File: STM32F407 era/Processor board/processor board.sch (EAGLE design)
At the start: 27 parts, among them Q1 8 MHz, X1 MINI-USB-SCHIELD-32005-201

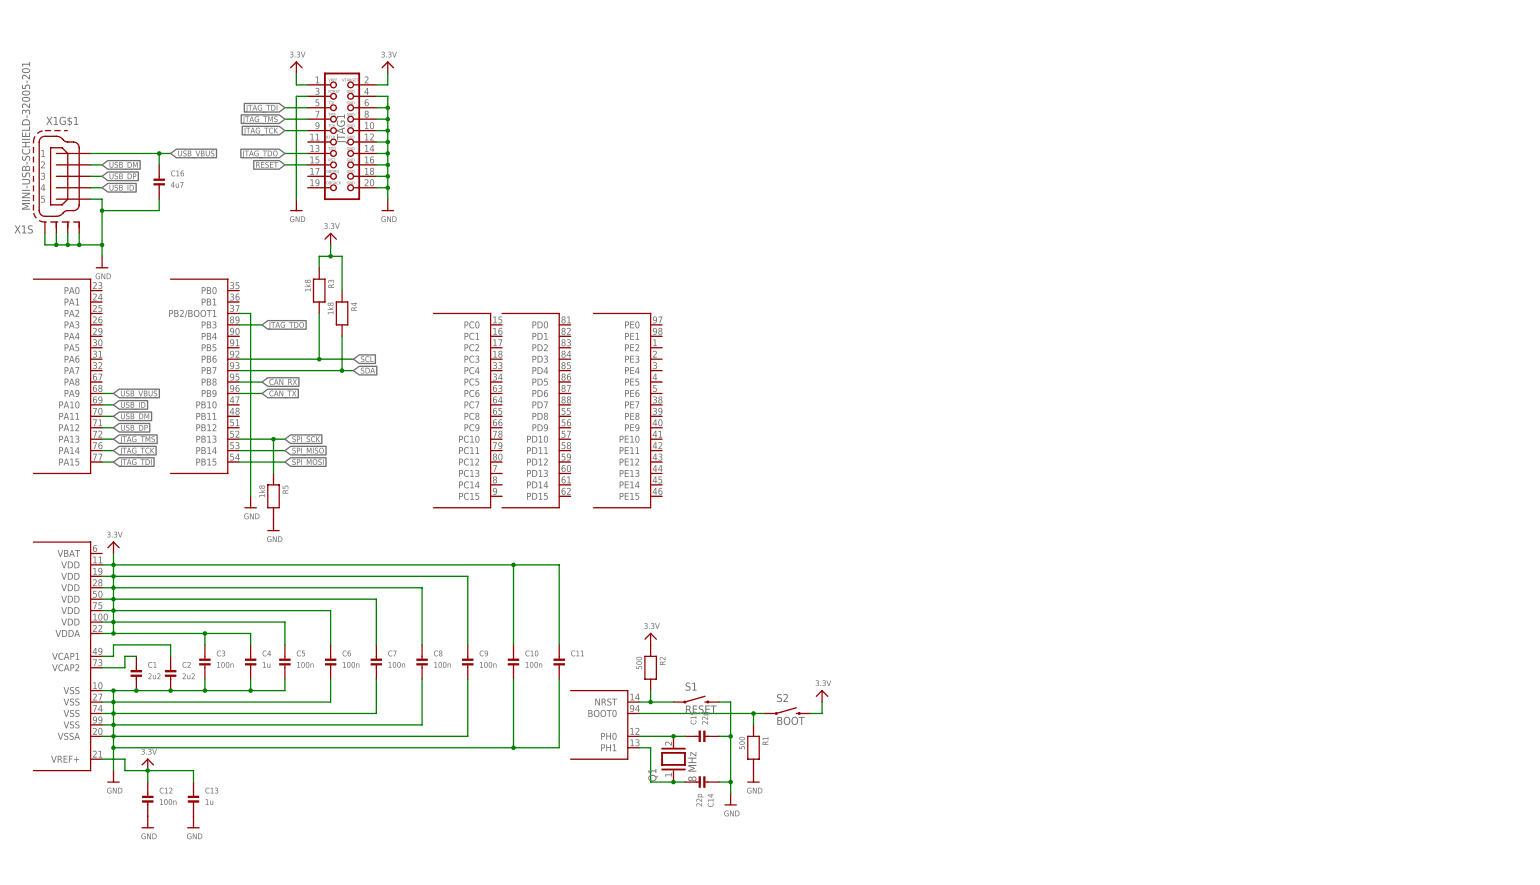
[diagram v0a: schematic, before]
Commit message: continued work on processor board
started doing the layout for the board and startet to add the
interfacing pin rows.
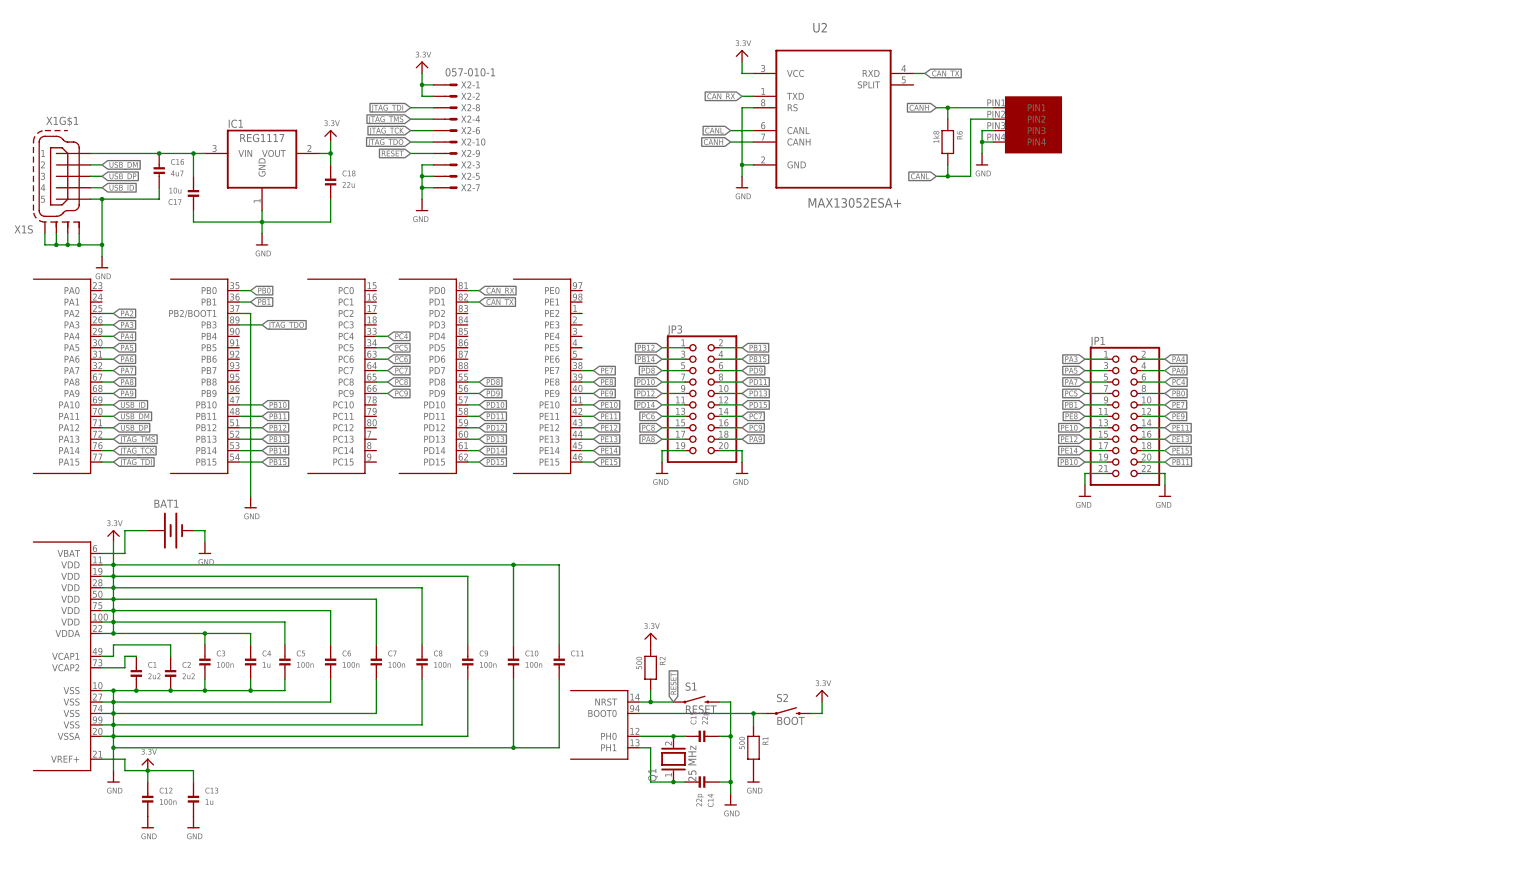
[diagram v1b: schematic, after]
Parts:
- removed JTAG1: JTAG-ARM, microbuilder:JTAG-ARM
- removed R3, R4, R5: 1k8, microbuilder:RESISTOR_0402MP
- added BAT1: (no value), SparkFun-Electromechanical:BATTERY12PTH
- added C17: 10u, microbuilder:CAP_CERAMIC_0603MP
- added C18: 22u, microbuilder:CAP_CERAMIC_0603MP
- added IC1: REG1117, burr-brown:REG1117
- added JP1: (no value), pinhead:PINHD-2X11
- added JP3: (no value), pinhead:PINHD-2X10
- added R6: 1k8, microbuilder:RESISTOR_0402MP
- added U$23: MICROFIT4, unicorn:MICROFIT4
- added U2: MAX13052ESA+, Maxim_By_element14_Batch_1:MAX13052ESA+
- added X2: 057-010-1, con-panduit:057-010-1
- Q1: value 8 MHz -> 25 MHz
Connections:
- removed net N$5: R2.2, S1.1, U1G$7.NRST
- removed net SCL: R3.2, U1G$3.PB6
- removed net SDA: R4.2, U1G$3.PB7
- removed net SPI_MISO: U1G$3.PB14
- removed net SPI_MOSI: U1G$3.PB15
- removed net SPI_SCK: R5.1, U1G$3.PB13
- new net CANH: R6.1, U$23.PIN1, U2.CANH
- new net CANL: R6.2, U$23.PIN2, U2.CANL
- new net N$6: BAT1.+, U1G$1.VBAT
- new net PA2: U1G$2.PA2
- new net PA3: JP1.1, U1G$2.PA3
- new net PA4: JP1.2, U1G$2.PA4
- new net PA5: JP1.3, U1G$2.PA5
- new net PA6: JP1.4, U1G$2.PA6
- new net PA7: JP1.5, U1G$2.PA7
- new net PA8: JP3.17, U1G$2.PA8
- new net PA9: JP3.18, U1G$2.PA9
- new net PB0: JP1.8, U1G$3.PB0
- new net PB1: JP1.9, U1G$3.PB1
- new net PB10: JP1.19, U1G$3.PB10
- new net PB11: JP1.20, U1G$3.PB11
- new net PB12: JP3.1, U1G$3.PB12
- new net PB13: JP3.2, U1G$3.PB13
- new net PB14: JP3.3, U1G$3.PB14
- new net PB15: JP3.4, U1G$3.PB15
- new net PC4: JP1.6, U1G$4.PC4
- new net PC5: JP1.7, U1G$4.PC5
- new net PC6: JP3.13, U1G$4.PC6
- new net PC7: JP3.14, U1G$4.PC7
- new net PC8: JP3.15, U1G$4.PC8
- new net PC9: JP3.16, U1G$4.PC9
- new net PD10: JP3.7, U1G$5.PD10
- new net PD11: JP3.8, U1G$5.PD11
- new net PD12: JP3.9, U1G$5.PD12
- new net PD13: JP3.10, U1G$5.PD13
- new net PD14: JP3.11, U1G$5.PD14
- new net PD15: JP3.12, U1G$5.PD15
- new net PD8: JP3.5, U1G$5.PD8
- new net PD9: JP3.6, U1G$5.PD9
- new net PE10: JP1.13, U1G$6.PE10
- new net PE11: JP1.14, U1G$6.PE11
- new net PE12: JP1.15, U1G$6.PE12
- new net PE13: JP1.16, U1G$6.PE13
- new net PE14: JP1.17, U1G$6.PE14
- new net PE15: JP1.18, U1G$6.PE15
- new net PE7: JP1.10, U1G$6.PE7
- new net PE8: JP1.11, U1G$6.PE8
- new net PE9: JP1.12, U1G$6.PE9
- net 3.3V: now also C18.P$1, IC1.VOUT, U2.VCC, X2-1.S, X2-2.S; no longer JTAG1.1, JTAG1.2, R3.1, R4.1
- net CAN_RX: now also U1G$5.PD0, U2.TXD; no longer U1G$3.PB8
- net CAN_TX: now also U1G$5.PD1, U2.RXD; no longer U1G$3.PB9
- net GND: now also BAT1.-, C17.P$1, C18.P$2, IC1.GND, JP1.21, JP1.22, JP3.19, JP3.20, U$23.PIN3, U$23.PIN4, U2.GND, U2.RS, X2-3.S, X2-5.S, X2-7.S; no longer JTAG1.10, JTAG1.12, JTAG1.14, JTAG1.16, JTAG1.18, JTAG1.20, JTAG1.3, JTAG1.4, JTAG1.6, JTAG1.8, R5.2
- net JTAG_TCK: now also X2-6.S; no longer JTAG1.9
- net JTAG_TDI: now also X2-8.S; no longer JTAG1.5
- net JTAG_TDO: now also X2-10.S; no longer JTAG1.13
- net JTAG_TMS: now also X2-4.S; no longer JTAG1.7
- net RESET: now also R2.2, S1.1, U1G$7.NRST, X2-9.S; no longer JTAG1.15
- net USB_VBUS: now also C17.P$2, IC1.VIN; no longer U1G$2.PA9
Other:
- moved on the sheet: C16

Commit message: finished v 0.1 of processor board layout
TA DAAAAAA!
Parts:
- removed Q1: 25 MHz, special:XTAL/S
- added C19, C20: 6p8, microbuilder:CAP_CERAMIC_0402MP
- added JP2: (no value), pinhead:PINHD-2X11
- added JP4: (no value), pinhead:PINHD-2X8
- added LED1: (no value), led:LEDCHIPLED_1206
- added R3: 100, microbuilder:RESISTOR_0402MP
- added TP1: (no value), microbuilder:TESTPOINT0.1"
- added Y1: 25 MHz, microbuilder:CRYSTAL2.5X2.0MM
- added Y2: 32.768KHz, microbuilder:CRYSTAL32.768
- BAT1: value (none) -> CR1220
- C11: value (none) -> 4u7
- JP3: device pinhead:PINHD-2X10 -> pinhead:PINHD-2X9
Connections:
- new net N$5: LED1.A, R3.2
- new net PA0: JP4.13, U1G$2.PA0
- new net PA1: JP4.14, U1G$2.PA1
- new net PB4: JP3.10, U1G$3.PB4
- new net PB5: JP3.11, U1G$3.PB5
- new net PB6: JP3.12, U1G$3.PB6
- new net PB7: JP3.13, U1G$3.PB7
- new net PB8: JP3.14, U1G$3.PB8
- new net PB9: JP3.15, U1G$3.PB9
- new net PC0: JP4.9, U1G$4.PC0
- new net PC1: JP4.10, U1G$4.PC1
- new net PC10: JP3.1, U1G$4.PC10
- new net PC11: JP3.2, U1G$4.PC11
- new net PC12: JP3.3, U1G$4.PC12
- new net PC13: JP4.6, U1G$4.PC13
- new net PC14: C19.P$1, U1G$4.PC14, Y2.2
- new net PC15: C20.P$1, U1G$4.PC15, Y2.1
- new net PC2: JP4.11, U1G$4.PC2
- new net PC3: JP4.12, U1G$4.PC3
- new net PD2: JP3.4, U1G$5.PD2
- new net PD3: JP3.5, U1G$5.PD3
- new net PD4: JP3.6, U1G$5.PD4
- new net PD5: JP3.7, U1G$5.PD5
- new net PD6: JP3.8, U1G$5.PD6
- new net PD7: JP3.9, U1G$5.PD7
- new net PE0: JP3.16, U1G$6.PE0
- new net PE1: JP3.17, U1G$6.PE1
- new net PE2: JP4.1, U1G$6.PE2
- new net PE3: JP4.2, U1G$6.PE3
- new net PE4: JP4.3, U1G$6.PE4
- new net PE5: JP4.4, U1G$6.PE5
- new net PE6: JP4.5, U1G$6.PE6
- net 3.3V: now also JP2.21, JP2.22, R3.1
- net GND: now also C19.P$2, C20.P$2, JP2.19, JP2.20, JP3.18, JP4.16, JP4.7, JP4.8, LED1.C, TP1.P$1; no longer JP3.19, JP3.20
- net N$1: now also Y1.2; no longer Q1.2
- net N$11: now also Y1.1; no longer Q1.1
- net PA2: now also JP4.15
- net PA8: now also JP2.17; no longer JP3.17
- net PA9: now also JP2.18; no longer JP3.18
- net PB12: now also JP2.1; no longer JP3.1
- net PB13: now also JP2.2; no longer JP3.2
- net PB14: now also JP2.3; no longer JP3.3
- net PB15: now also JP2.4; no longer JP3.4
- net PC6: now also JP2.13; no longer JP3.13
- net PC7: now also JP2.14; no longer JP3.14
- net PC8: now also JP2.15; no longer JP3.15
- net PC9: now also JP2.16; no longer JP3.16
- net PD10: now also JP2.7; no longer JP3.7
- net PD11: now also JP2.8; no longer JP3.8
- net PD12: now also JP2.9; no longer JP3.9
- net PD13: now also JP2.10; no longer JP3.10
- net PD14: now also JP2.11; no longer JP3.11
- net PD15: now also JP2.12; no longer JP3.12
- net PD8: now also JP2.5; no longer JP3.5
- net PD9: now also JP2.6; no longer JP3.6
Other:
- moved on the sheet: JP1, X2-1, X2-10, X2-2, X2-3, X2-4, X2-5, X2-6, X2-7, X2-8, X2-9

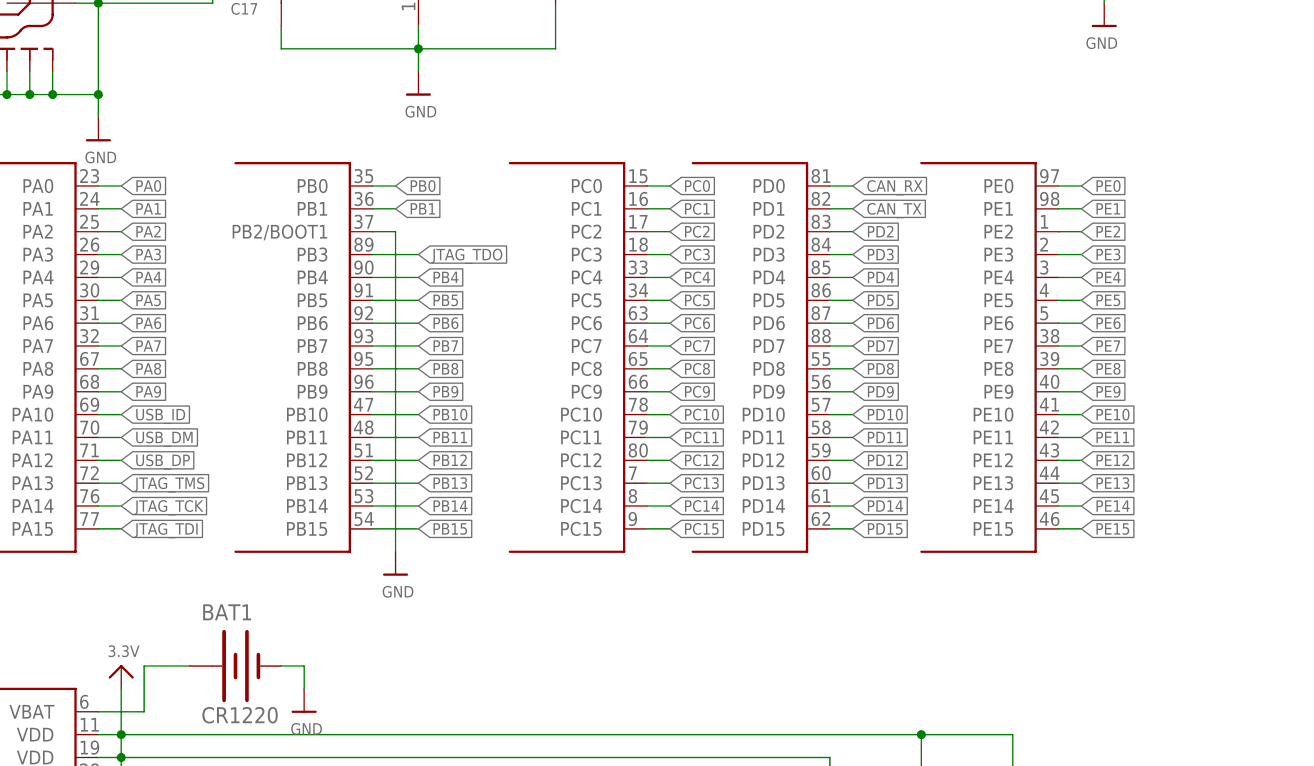
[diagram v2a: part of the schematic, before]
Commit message: finished v 0.5 of processsor board
Did some cleaning of the pin busses, and some small components
placements cleanup.
Added Unicorn Logo and board name to silkscreen
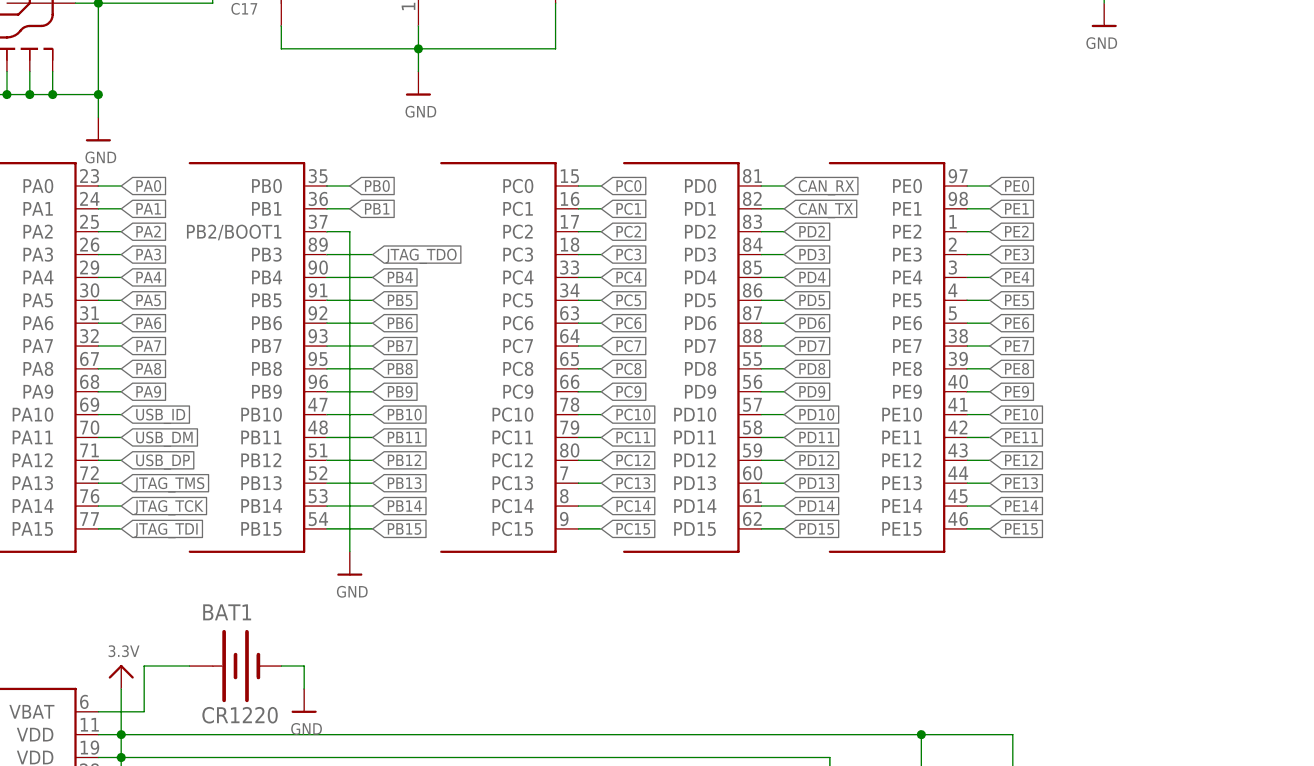
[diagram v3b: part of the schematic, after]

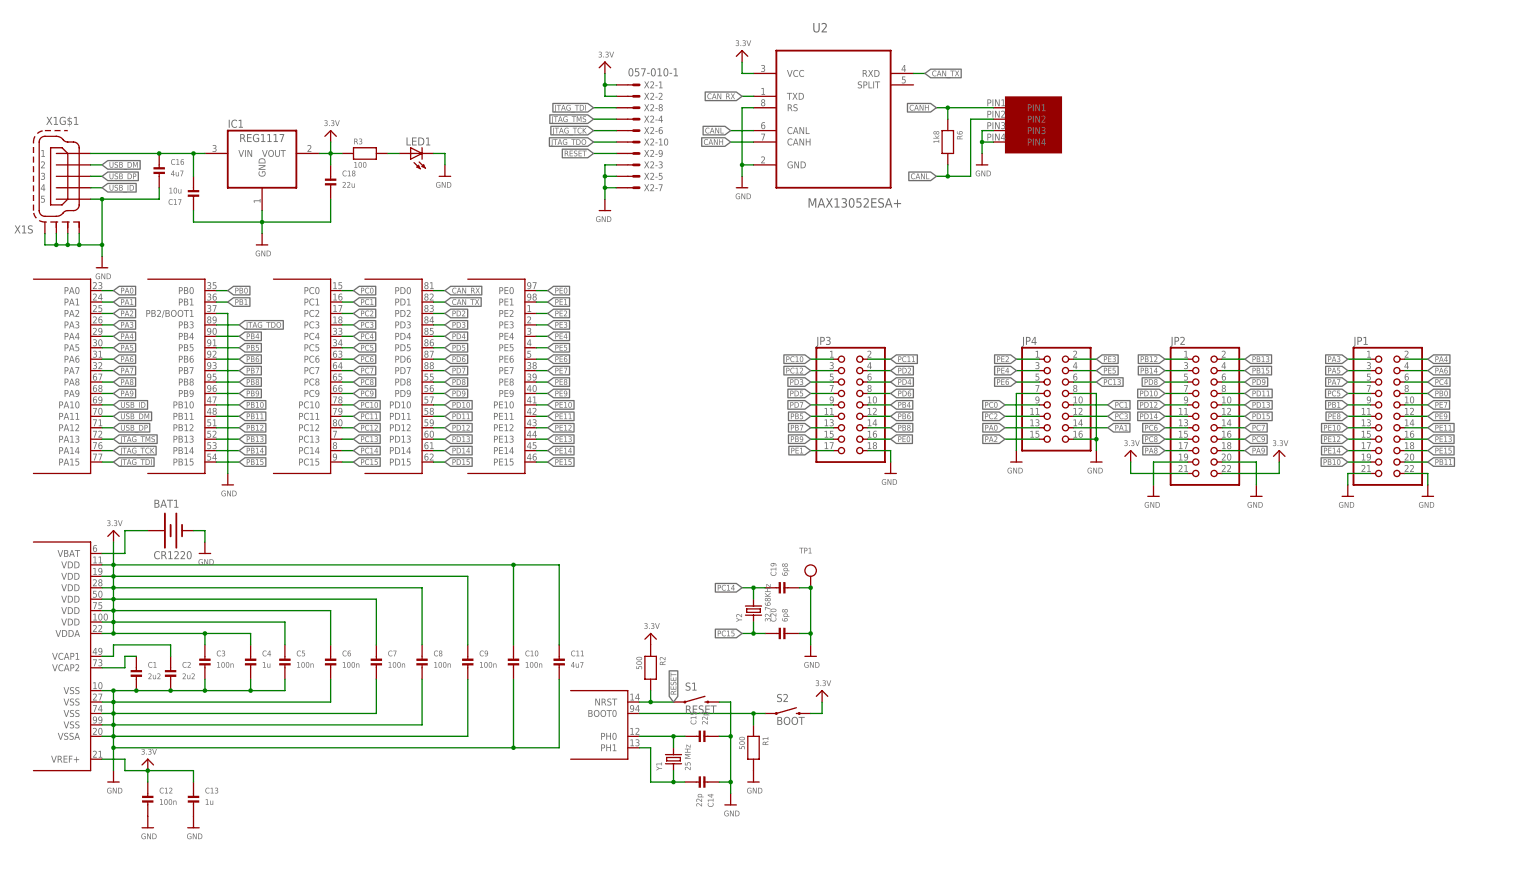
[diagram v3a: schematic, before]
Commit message: CPU board schematic cleanup
cleaned up the schematic for easier reading
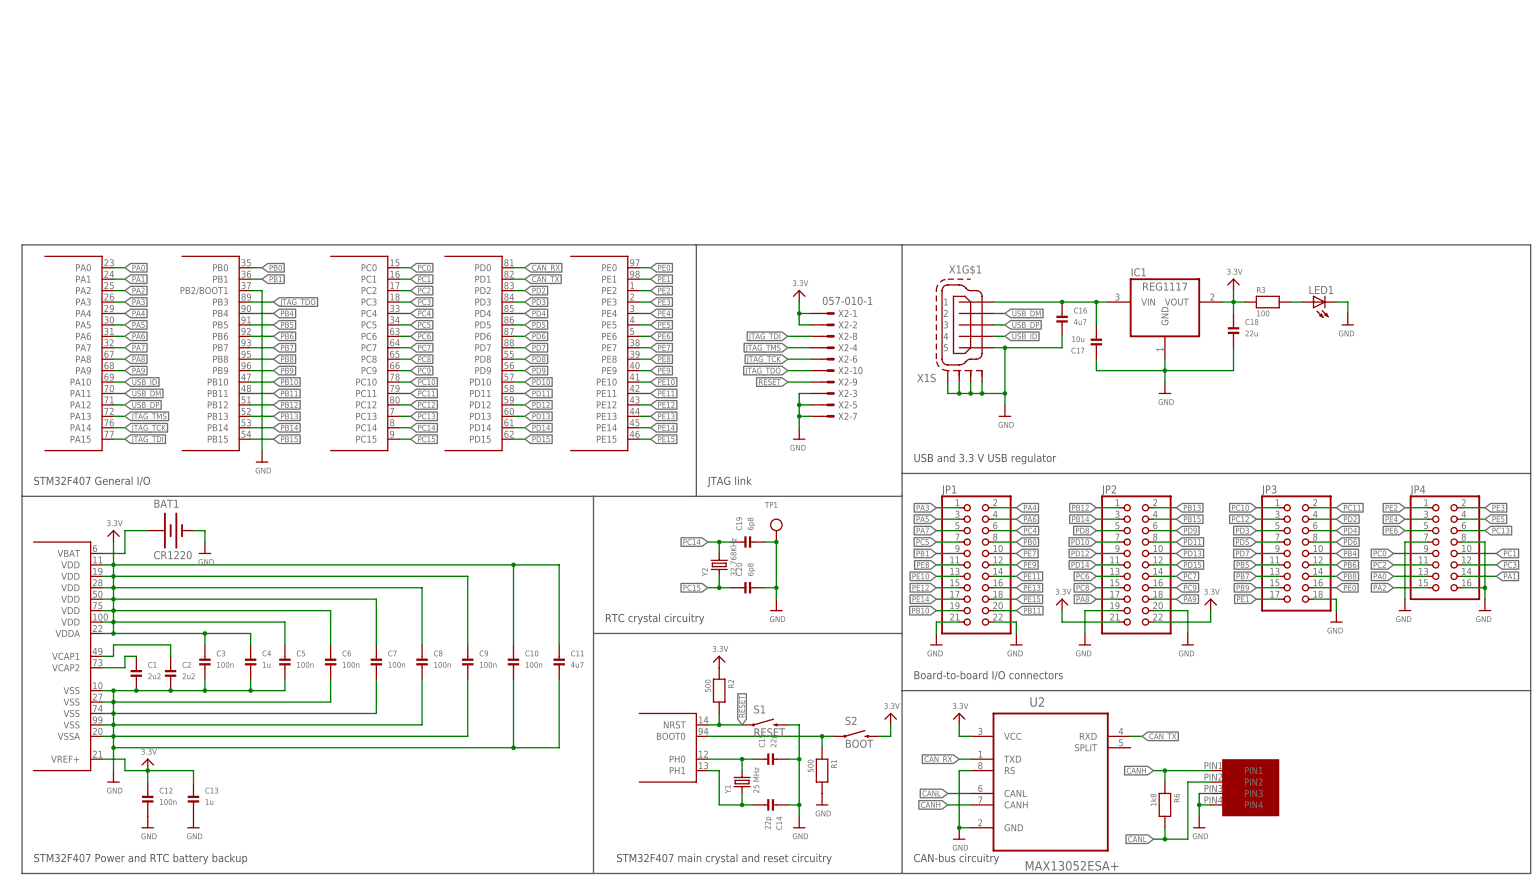
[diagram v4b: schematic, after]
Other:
- note added: "Board-to-board I/O connectors"
- note added: "CAN-bus circuitry"
- note added: "JTAG link"
- note added: "RTC crystal circuitry"
- note added: "STM32F407 General I/O"
- note added: "STM32F407 Power and RTC battery backup"
- note added: "STM32F407 main crystal and reset circuitry"
- note added: "USB and 3.3 V USB regulator"
- moved on the sheet: C14, C15, C16, C17, C18, C19, C20, IC1, JP1, JP2, JP3, JP4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

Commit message: last layout update for V1
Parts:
- added JP6: (no value), pinhead:PINHD-1X1
- C1, C10, C11, C12, C13, C14, C15, C19, C2, C20, C3, C4, C5, C6, C7, C8, C9: device microbuilder:CAP_CERAMIC_0402MP -> microbuilder:CAP_CERAMIC_0603MP
- R1, R2, R3, R6: device microbuilder:RESISTOR_0402MP -> microbuilder:RESISTOR_0603MP
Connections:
- net GND: now also JP1.19, JP1.20, JP6.1; no longer JP1.21, JP1.22
- net PB10: now also JP1.21; no longer JP1.19
- net PB11: now also JP1.22; no longer JP1.20
